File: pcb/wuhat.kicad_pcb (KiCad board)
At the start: 2 copper layers, 65 x 56 mm, 202 parts, among them J1 GPIOcon, U1 MCP3002, U3 ID

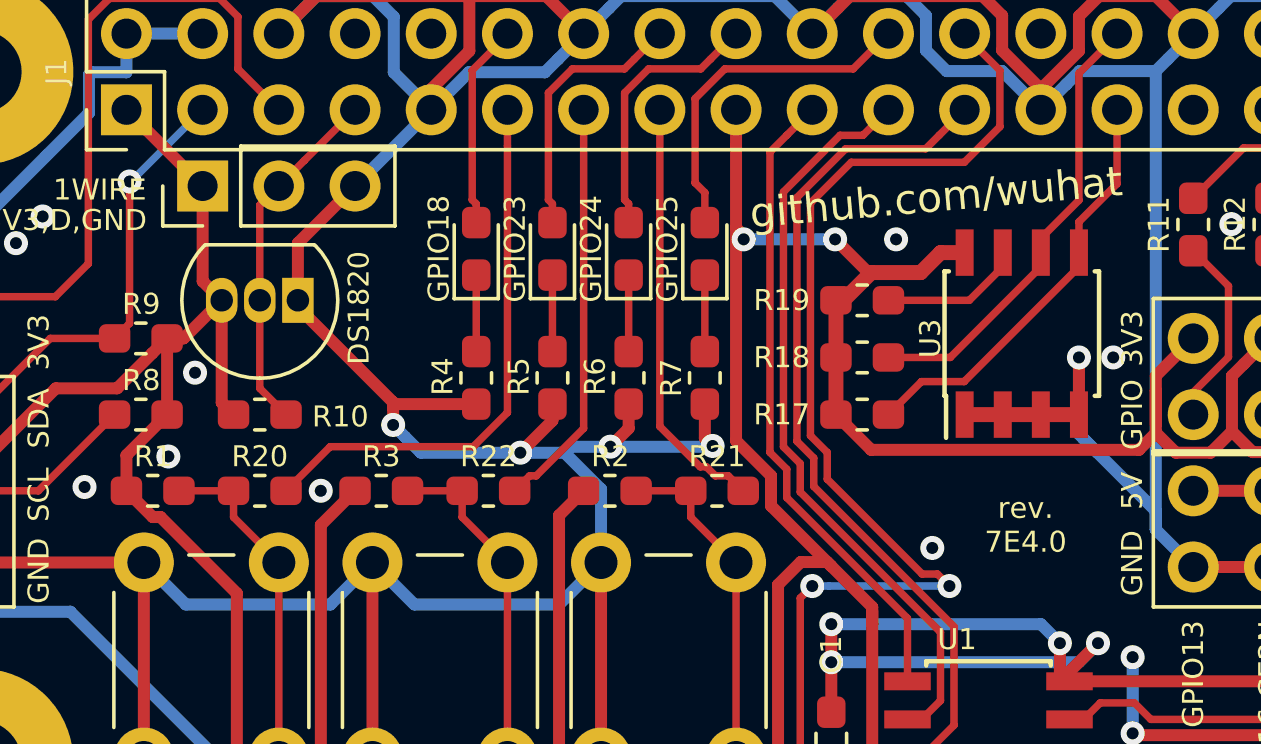
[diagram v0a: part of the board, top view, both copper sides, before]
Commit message: modified DS1820 footprint
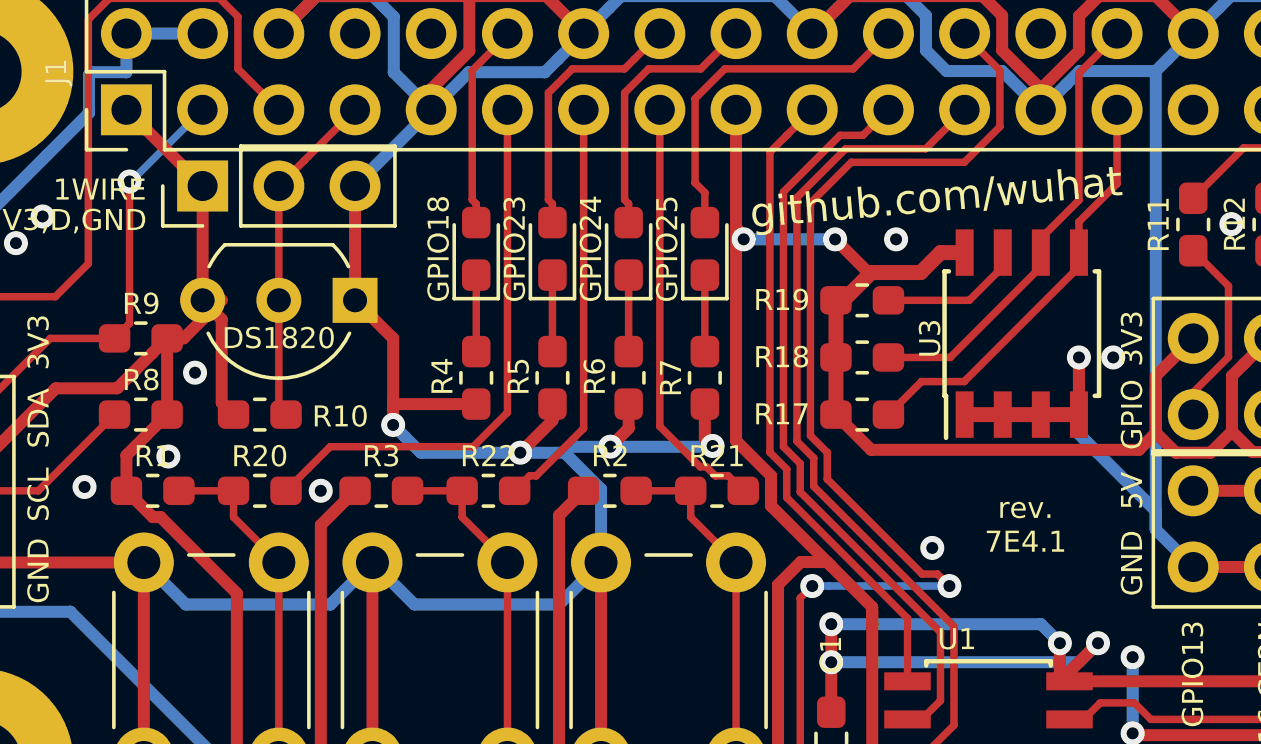
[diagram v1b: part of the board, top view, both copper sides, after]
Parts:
- DS1820: footprint Package_TO_SOT_THT:TO-92_Inline -> Package_TO_SOT_THT:TO-92_Inline_Wide
- moved DS1820 1.91 mm to (117.6, 106.8)
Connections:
- J1 pad 10: (no net) -> Net-(J1-Pad10)
- J1 pad 26: (no net) -> Net-(J1-Pad26)
- J1 pad 29: (no net) -> Net-(J1-Pad29)
- J1 pad 31: (no net) -> Net-(J1-Pad31)
- J1 pad 32: (no net) -> Net-(J1-Pad32)
- J1 pad 8: (no net) -> Net-(J1-Pad8)
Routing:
- net GND: track 331.7 -> 330.1 mm
- net /GPIO4_1WIRE: track 11.8 -> 11.3 mm
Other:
- board text added: "rev. 7E4.1"
- board text removed: "rev. 7E4.0"
